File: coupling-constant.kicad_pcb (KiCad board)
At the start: 2 copper layers, 84.5 x 30.5 mm, 36 parts, among them J1 Input, J102 Output, J104 DC IN, U101 TL072, U102 TC1044SxOA

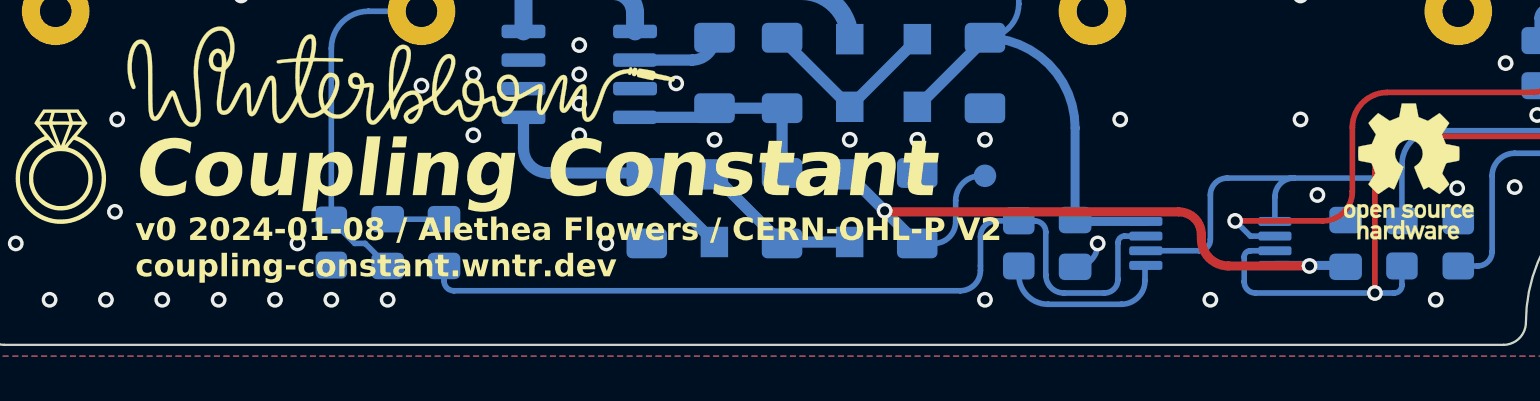
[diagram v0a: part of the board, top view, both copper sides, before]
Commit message: v1, fixup op amp inputs
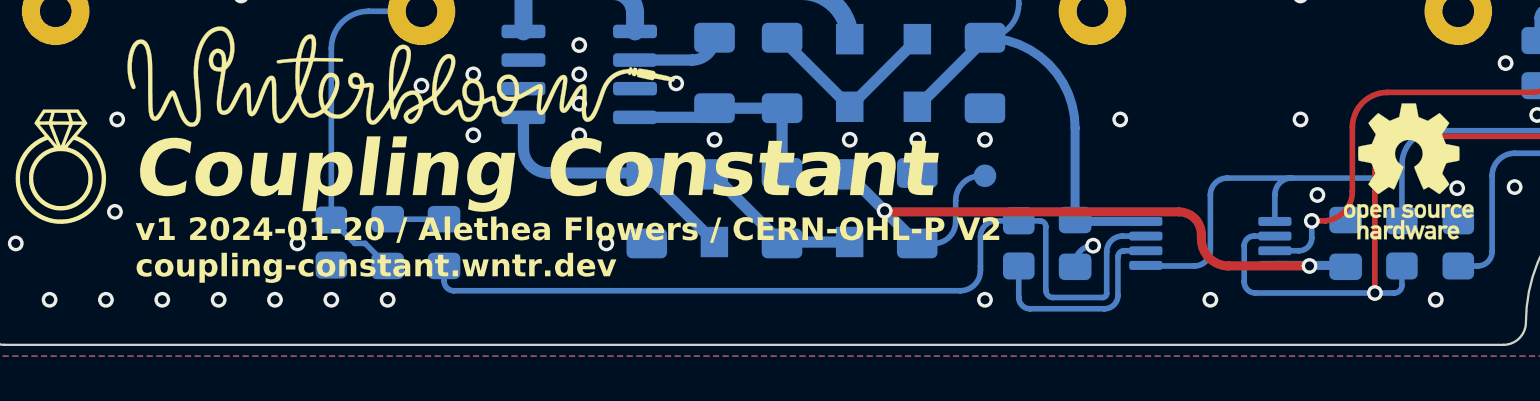
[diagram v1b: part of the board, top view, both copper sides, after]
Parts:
- C103: value 4.7u -> 4u7
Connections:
- C101 pad 2: Net-(U101A--) -> Net-(U101A-+)
- C104 pad 1: Net-(U101A-+) -> Net-(U101A--)
- C104 pad 2: Net-(U101B--) -> Net-(U101B-+)
- C105 pad 1: Net-(U101B-+) -> Net-(U101B--)
- R101 pad 1: Net-(U101A--) -> Net-(U101A-+)
- R103 pad 1: Net-(U101A-+) -> Net-(U101A--)
- R103 pad 2: Net-(U101B--) -> Net-(U101B-+)
- R104 pad 2: Net-(U101A-+) -> Net-(U101A--)
- U101 pad 1: Net-(U101B--) -> Net-(U101B-+)
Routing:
- net Net-(U101B-+): track 7.94 -> 30.4 mm
- net Net-(U101B--): track 29.9 -> 9.47 mm
- net Net-(U101A-+): track 33.6 -> 26.4 mm
- net Net-(U101A--): track 29.1 -> 34.2 mm
- net Net-(C105-Pad2): track 39.1 -> 39.9 mm

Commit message: finalize v1
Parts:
- added D6: Power, LED_THT:LED_D3.0mm, B.Cu at (153.2, 112.7)
- added R8: 4k7, winterbloom:R_0805_HandSolder, B.Cu at (147.5, 112.7)
- C10: renamed from C104; footprint winterbloom:R_0805_HandSolder -> winterbloom:C_0805_HandSolder
- C13: renamed from C105; footprint winterbloom:R_0805_HandSolder -> winterbloom:C_0805_HandSolder
- C9: renamed from C103; footprint winterbloom:R_0805_HandSolder -> winterbloom:C_0805_HandSolder
- R6: renamed from R109; footprint winterbloom:C_0805_HandSolder -> winterbloom:R_0805_HandSolder
- TP1: renamed from TP102; moved to F.Cu
- TP2: renamed from TP103; moved to F.Cu
- U2: renamed from U101; footprint Package_SO:TSSOP-8_4.4x3mm_P0.65mm -> Package_SO:SOIC-8_3.9x4.9mm_P1.27mm
- moved R2 61.1 mm to (138.6, 117.8), turned to 90 degrees
- moved R1 57.5 mm to (136.1, 117.8), turned to 90 degrees
- moved R3 53.9 mm to (141.1, 117.8), turned to -90 degrees
- moved C8 53.9 mm to (143.6, 117.8)
- moved R4 50.2 mm to (148.6, 117.8), turned to -90 degrees
- moved J2 46.1 mm to (143.1, 107.2)
- moved J3 46.1 mm to (189.1, 107.2)
- moved C10 45.3 mm to (151.1, 117.8), turned to 90 degrees
- moved C9 43.1 mm to (146.1, 117.8), turned to 90 degrees
- moved R7 39.2 mm to (178.1, 117.8)
- moved R6 34.2 mm to (175.6, 117.8), turned to -90 degrees
- moved R5 33.1 mm to (153.6, 117.8)
- moved C14 29.2 mm to (173.1, 117.8), turned to -90 degrees
- moved C11 16.2 mm to (168.1, 117.8)
- moved C12 16.2 mm to (156.1, 117.8)
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- gave numbers to parts that had none: 1
- renumbered C102 to C1, C113 to C11, C106 to C12, C114 to C14, C108 to C2, C111 to C3, C109 to C4, C110 to C5, C107 to C6, C112 to C7, C101 to C8, D101 to D1, D105 to D2, D103 to D3, D107 to D4, D106 to D5, J104 to J1, J1 to J2, J102 to J3, R101 to R1, R105 to R2, R102 to R3, R104 to R4, R103 to R5, R108 to R7, U102 to U1
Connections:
- C10 pad 1: Net-(U101A--) -> Net-(U2B--)
- C10 pad 2: Net-(U101B-+) -> Net-(U2A-+)
- C13 pad 1: Net-(U101B--) -> Net-(U2A--)
- C13 pad 2: Net-(C105-Pad2) -> Net-(C13-Pad2)
- C14 pad 1: Net-(C105-Pad2) -> Net-(C13-Pad2)
- C8 pad 2: Net-(U101A-+) -> Net-(U2B-+)
- R1 pad 1: Net-(U101A-+) -> Net-(U2B-+)
- R4 pad 2: Net-(U101A--) -> Net-(U2B--)
- R5 pad 1: Net-(U101A--) -> Net-(U2B--)
- R5 pad 2: Net-(U101B-+) -> Net-(U2A-+)
- U2 pad 1: Net-(U101B-+) -> Net-(C13-Pad2)
- U2 pad 2: Net-(U101A--) -> Net-(U2A--)
- U2 pad 3: Net-(U101A-+) -> Net-(U2A-+)
- U2 pad 5: Net-(U101B-+) -> Net-(U2B-+)
- U2 pad 6: Net-(U101B--) -> Net-(U2B--)
- U2 pad 7: Net-(C105-Pad2) -> Net-(U2A-+)
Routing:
- net Net-(C105-Pad2): track 39.9 -> 0.00 mm
- net Net-(U101A--): track 34.2 -> 0.00 mm, vias 2 -> 0
- net Net-(U2B-+): track 0.00 -> 30.7 mm, vias 0 -> 3
- net Net-(U101B-+): track 30.4 -> 0.00 mm
- net Net-(U101A-+): track 26.4 -> 0.00 mm, vias 2 -> 0
- net Net-(U2A-+): track 0.00 -> 19.1 mm
- net VEE: track 32.8 -> 15.3 mm
- net Net-(U2B--): track 0.00 -> 12.7 mm
- net Net-(C9-Pad2): track 14.8 -> 2.52 mm
- net Net-(C13-Pad2): track 0.00 -> 9.90 mm
- net Net-(U101B--): track 9.47 -> 0.00 mm
- net Net-(U2A--): track 0.00 -> 6.82 mm
- net +9V: track 34.5 -> 41.2 mm
- net Net-(U1-CAP-): track 9.62 -> 14.9 mm
- net /guitar in: track 7.77 -> 12.4 mm
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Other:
- board size 84.5 x 30.5 mm -> 72.5 x 33.5 mm
- board text added: "BUFFER OUT"
- board text added: "GUITAR IN"
